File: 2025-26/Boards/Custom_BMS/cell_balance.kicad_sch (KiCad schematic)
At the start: 34 parts

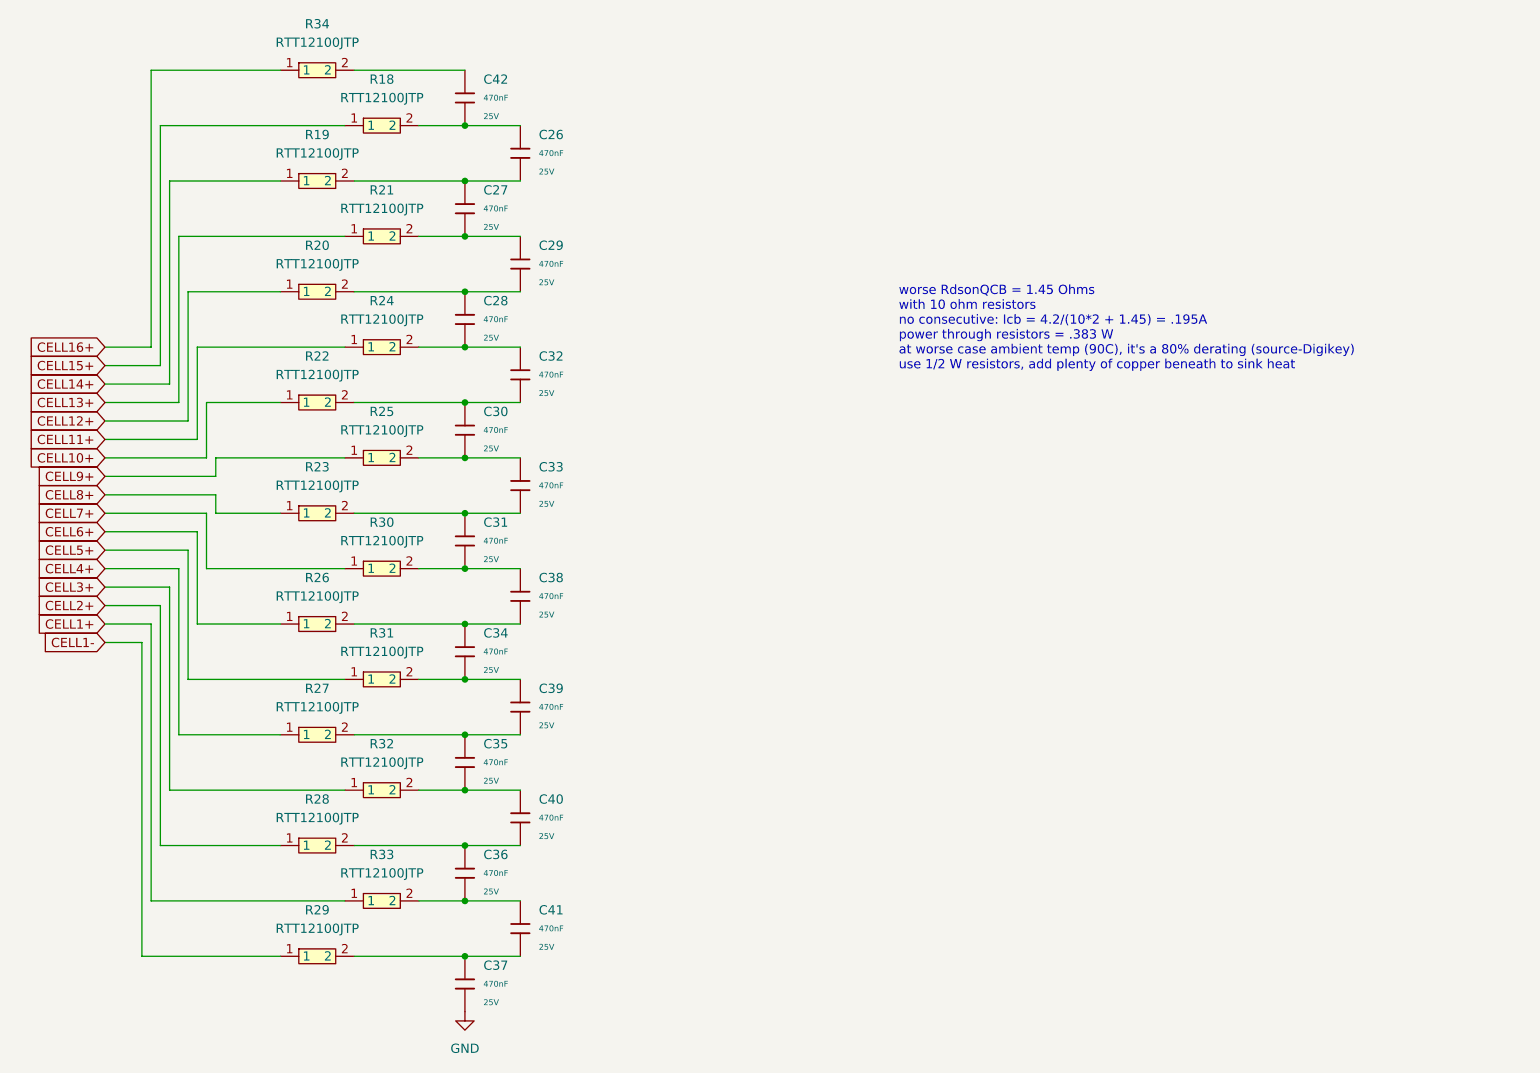
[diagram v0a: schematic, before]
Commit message: fixed some net names
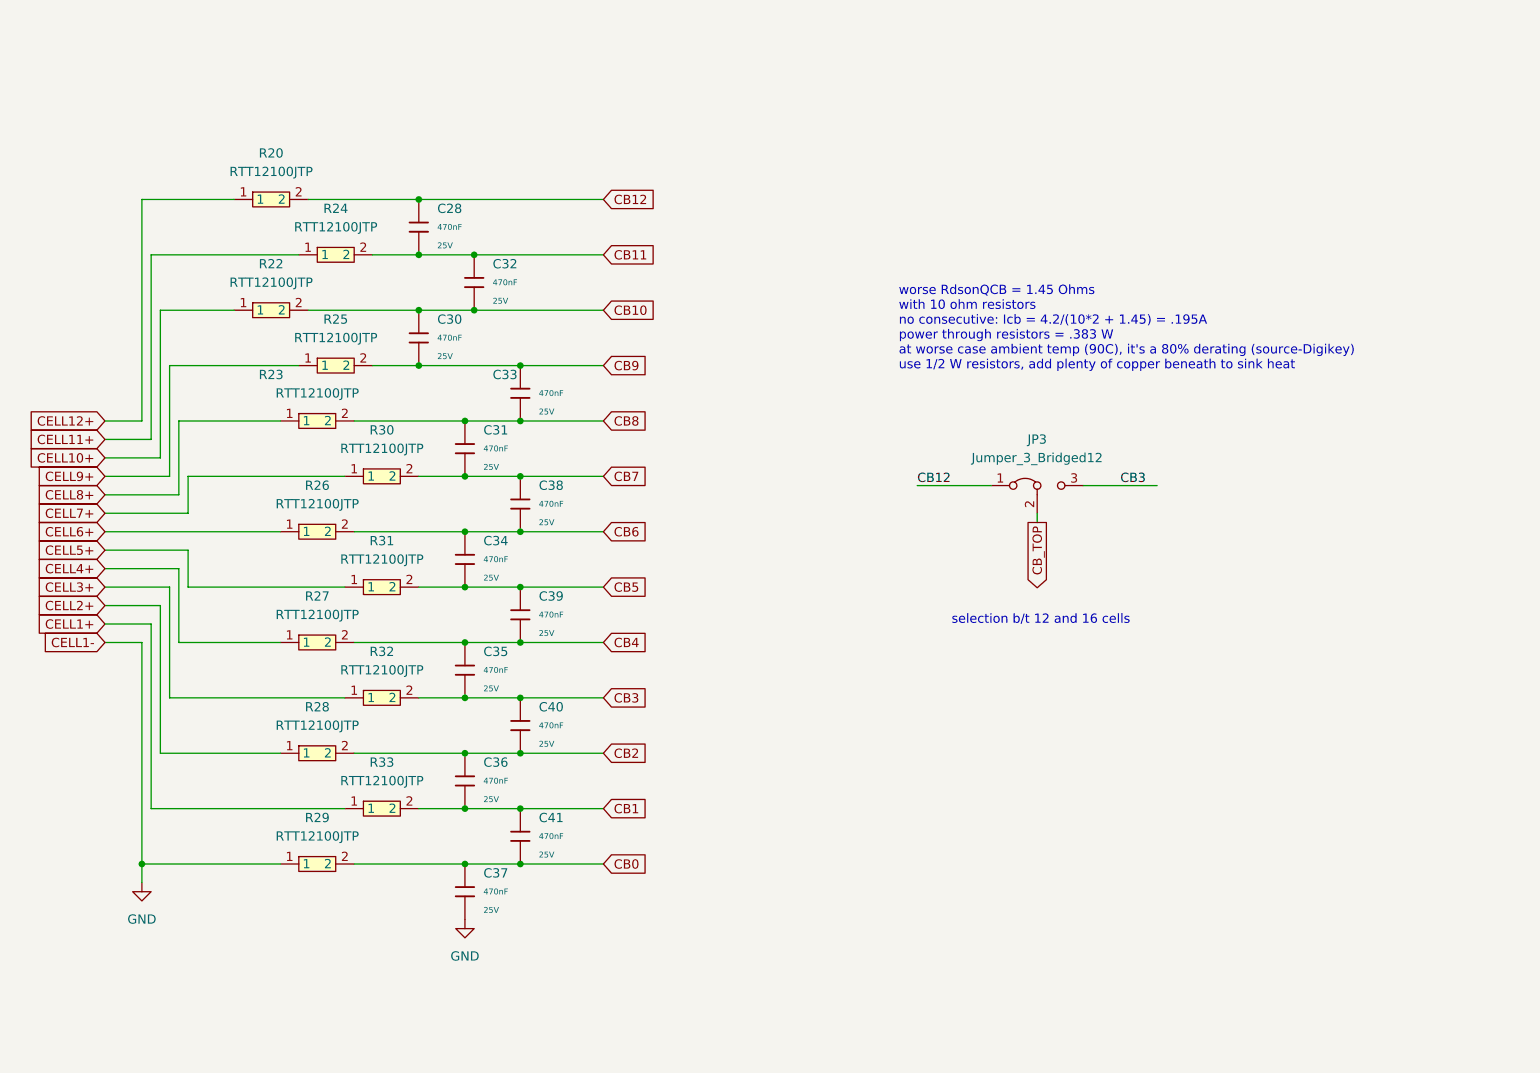
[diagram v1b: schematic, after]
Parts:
- removed C26, C27, C29, C42: 470nF, PCM_JLCPCB:C_0603, symbol PCM_JLCPCB-Capacitors:0603,470nF
- removed R18, R19, R21, R34: RTT12100JTP, easyeda2kicad:R1210, symbol easyeda2kicad:RTT12100JTP
- added JP3: Jumper_3_Bridged12, symbol Jumper:Jumper_3_Bridged12
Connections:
- net CELL1- is gone; now on net GND: R29.1
- net CB6: now reaches C34.1, C38.2, R26.2
- net CB8: now reaches C31.1, C33.2, R23.2
- net CB12: now reaches C28.1, R20.2
- net CB12: now also JP3.1 (A)
- net CB10: now reaches C30.1, C32.2, R22.2
- net CB3: now reaches C35.2, C40.1, R32.2
- net CB3: now also JP3.3 (B)
- net CB2: now reaches C36.1, C40.2, R28.2
- net CB9: now reaches C30.2, C33.1, R25.2
- net CB7: now reaches C31.2, C38.1, R30.2
- net CB11: now reaches C28.2, C32.1, R24.2
- net CB4: now reaches C35.1, C39.2, R27.2
- net CB5: now reaches C34.2, C39.1, R31.2
- net CB0: now reaches C37.1, C41.2, R29.2
- net CB1: now reaches C36.2, C41.1, R33.2
- new net CB_TOP: JP3.2 (C)
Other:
- note added: "selection b/t 12 and 16 cells"
- moved on the sheet: C28, C30, C31, C32, C33, C34, C35, C36, C37, C38, C39, C40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

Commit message: started layout
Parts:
- removed JP3: Jumper_3_Bridged12, symbol Jumper:Jumper_3_Bridged12
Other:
- note removed: "selection b/t 12 and 16 cells"
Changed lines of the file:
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@@
 		)
 	)
-	(text "selection b/t 12 and 16 cells"
-		(exclude_from_sim no)
-		(at 188.468 116.332 0)
-		(effects
-			(font
-				(size 1.27 1.27)
-			)
-		)
-	)
 	(junction
 		(at 109.22 127)
@@
 	(wire
 		(pts
-			(xy 194.31 97.79) (xy 204.47 97.79)
-		)
-		(stroke
-			(width 0)
-			(type default)
-		)
-	)
-	(wire
-		(pts
 			(xy 66.04 91.44) (xy 66.04 66.04)
 		)
@@
 	(wire
 		(pts
-			(xy 187.96 101.6) (xy 187.96 102.87)
-		)
-		(stroke
-			(width 0)
-			(type default)
-		)
-	)
-	(wire
-		(pts
 			(xy 69.85 88.9) (xy 69.85 99.06)
 		)
@@
 	(wire
 		(pts
-			(xy 171.45 97.79) (xy 181.61 97.79)
-		)
-		(stroke
-			(width 0)
-			(type default)
-		)
-	)
-	(wire
-		(pts
 			(xy 116.84 149.86) (xy 128.27 149.86)
 		)
@@
 		)
 	)
-	(label "CB3"
-		(at 199.39 97.79 0)
-		(effects
-			(font
-				(size 1.27 1.27)
-			)
-			(justify left bottom)
-		)
-	)
-	(label "CB12"
-		(at 171.45 97.79 0)
-		(effects
-			(font
-				(size 1.27 1.27)
-			)
-			(justify left bottom)
-		)
-	)
 	(global_label "CELL9+"
 		(shape input)
@@
 		)
 	)
-	(global_label "CB_TOP"
-		(shape output)
-		(at 187.96 102.87 270)
-		(fields_autoplaced yes)
-		(effects
-			(font
-				(size 1.27 1.27)
-			)
-			(justify right)
-		)
-		(property "Intersheetrefs" "${INTERSHEET_REFS}"
-			(at 187.96 112.9309 90)
-			(effects
-				(font
-					(size 1.27 1.27)
-				)
-				(justify right)
-				(hide yes)
-			)
-		)
-	)
 	(global_label "CB11"
 		(shape input)
@@
 					(unit 1)
 				)
-			)
-		)
-	)
-	(symbol
-		(lib_id "Jumper:Jumper_3_Bridged12")
-		(at 187.96 97.79 0)
-		(unit 1)
-		(exclude_from_sim no)
-		(in_bom no)
-		(on_board yes)
-		(dnp no)
-		(fields_autoplaced yes)
-		(property "Reference" "JP3"
-			(at 187.96 91.44 0)
-			(effects
-				(font
-					(size 1.27 1.27)
-				)
-			)
-		)
-		(property "Value" "Jumper_3_Bridged12"
-			(at 187.96 93.98 0)
-			(effects
-				(font
-					(size 1.27 1.27)
-				)
-			)
-		)
-		(property "Footprint" ""
-			(at 187.96 97.79 0)
-			(effects
-				(font
-					(size 1.27 1.27)
-				)
-				(hide yes)
-			)
-		)
-		(property "Datasheet" "~"
-			(at 187.96 97.79 0)
-			(effects
-				(font
-					(size 1.27 1.27)
-				)
-				(hide yes)
-			)
-		)
-		(property "Description" "Jumper, 3-pole, pins 1+2 closed/bridged"
-			(at 187.96 97.79 0)
-			(effects
-				(font
-					(size 1.27 1.27)
-				)
-				(hide yes)
-			)
-		)
-		(pin "2"
-		)
-		(pin "3"
-		)
-		(pin "1"
-		)
-		(instances
-			(project "Custom_BMS"
-				(path "/570d6d9c-ebf5-4f83-96f6-d3309a3e637d/e94a219a-300a-4436-8821-3bf884f472d1"
-					(reference "JP3")
-					(unit 1)
-				)

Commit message: more layout progress
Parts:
- added JP2: Jumper_3_Bridged12, Connector_PinHeader_2.00mm:PinHeader_1x03_P2.00mm_Vertical, symbol Jumper:Jumper_3_Bridged12
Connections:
- new net CB12+: JP2.1 (A)
- new net CB3+: JP2.3 (B)
- new net CB_TOP: JP2.2 (C)
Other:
- note added: "selection b/t 12 and 16 cells"
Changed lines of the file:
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@@
 		)
 	)
+	(text "selection b/t 12 and 16 cells"
+		(exclude_from_sim no)
+		(at 195.072 125.73 0)
+		(effects
+			(font
+				(size 1.27 1.27)
+			)
+		)
+	)
 	(junction
 		(at 109.22 127)
@@
 	(wire
 		(pts
+			(xy 176.53 104.14) (xy 186.69 104.14)
+		)
+		(stroke
+			(width 0)
+			(type default)
+		)
+	)
+	(wire
+		(pts
 			(xy 69.85 109.22) (xy 69.85 119.38)
 		)
@@
 	(wire
 		(pts
+			(xy 193.04 107.95) (xy 193.04 109.22)
+		)
+		(stroke
+			(width 0)
+			(type default)
+		)
+	)
+	(wire
+		(pts
 			(xy 59.69 93.98) (xy 67.31 93.98)
 		)
@@
 	(wire
 		(pts
+			(xy 199.39 104.14) (xy 209.55 104.14)
+		)
+		(stroke
+			(width 0)
+			(type default)
+		)
+	)
+	(wire
+		(pts
 			(xy 116.84 96.52) (xy 128.27 96.52)
 		)
@@
 		)
 	)
+	(label "CB3+"
+		(at 201.93 104.14 0)
+		(effects
+			(font
+				(size 1.27 1.27)
+			)
+			(justify left bottom)
+		)
+	)
+	(label "CB12+"
+		(at 176.53 104.14 0)
+		(effects
+			(font
+				(size 1.27 1.27)
+			)
+			(justify left bottom)
+		)
+	)
+	(global_label "CB_TOP"
+		(shape output)
+		(at 193.04 109.22 270)
+		(fields_autoplaced yes)
+		(effects
+			(font
+				(size 1.27 1.27)
+			)
+			(justify right)
+		)
+		(property "Intersheetrefs" "${INTERSHEET_REFS}"
+			(at 193.04 119.2809 90)
+			(effects
+				(font
+					(size 1.27 1.27)
+				)
+				(justify right)
+				(hide yes)
+			)
+		)
+	)
 	(global_label "CELL9+"
 		(shape input)
@@
 					(unit 1)
 				)
+			)
+		)
+	)
+	(symbol
+		(lib_id "Jumper:Jumper_3_Bridged12")
+		(at 193.04 104.14 0)
+		(unit 1)
+		(exclude_from_sim no)
+		(in_bom no)
+		(on_board yes)
+		(dnp no)
+		(fields_autoplaced yes)
+		(property "Reference" "JP2"
+			(at 193.04 97.79 0)
+			(effects
+				(font
+					(size 1.27 1.27)
+				)
+			)
+		)
+		(property "Value" "Jumper_3_Bridged12"
+			(at 193.04 100.33 0)
+			(effects
+				(font
+					(size 1.27 1.27)
+				)
+			)
+		)
+		(property "Footprint" "Connector_PinHeader_2.00mm:PinHeader_1x03_P2.00mm_Vertical"
+			(at 193.04 104.14 0)
+			(effects
+				(font
+					(size 1.27 1.27)
+				)
+				(hide yes)
+			)
+		)
+		(property "Datasheet" "~"
+			(at 193.04 104.14 0)
+			(effects
+				(font
+					(size 1.27 1.27)
+				)
+				(hide yes)
+			)
+		)
+		(property "Description" "Jumper, 3-pole, pins 1+2 closed/bridged"
+			(at 193.04 104.14 0)
+			(effects
+				(font
+					(size 1.27 1.27)
+				)
+				(hide yes)
+			)
+		)
+		(pin "2"
+		)
+		(pin "3"
+		)
+		(pin "1"
+		)
+		(instances
+			(project "Custom_BMS"
+				(path "/570d6d9c-ebf5-4f83-96f6-d3309a3e637d/e94a219a-300a-4436-8821-3bf884f472d1"
+					(reference "JP2")
+					(unit 1)
+				)

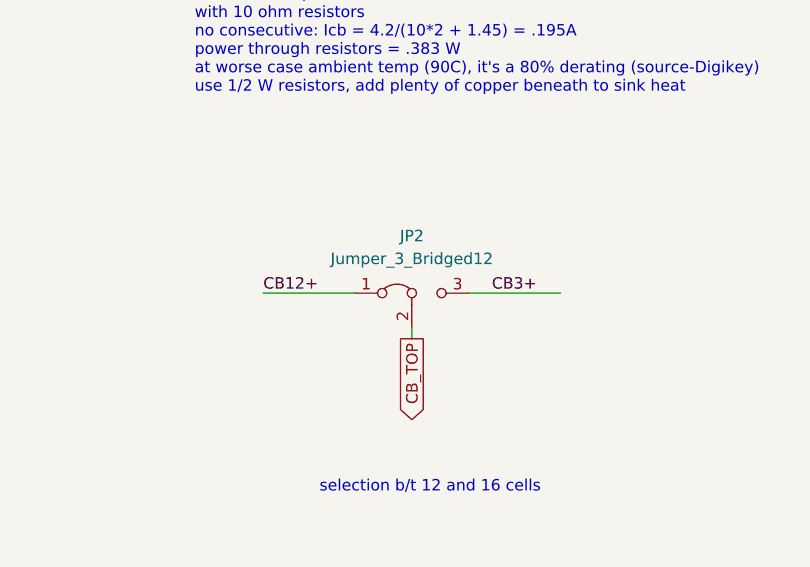
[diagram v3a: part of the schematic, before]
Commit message: finishe difrst draft layout
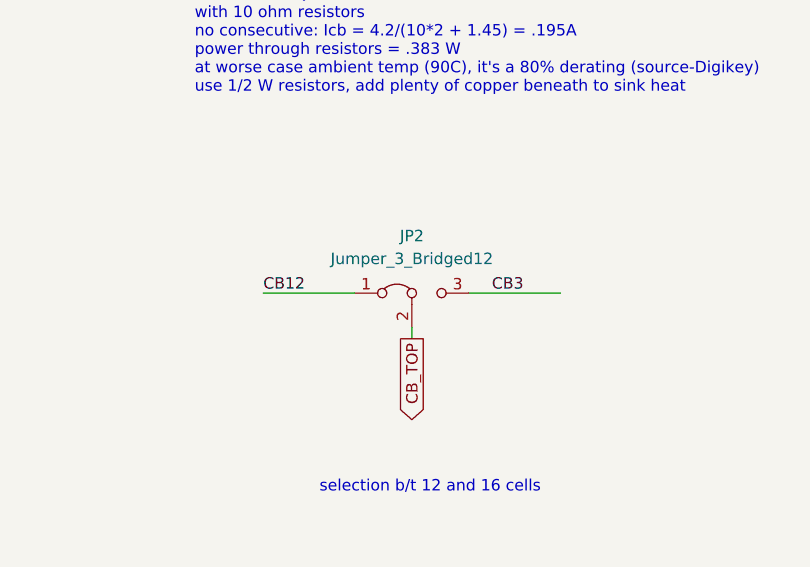
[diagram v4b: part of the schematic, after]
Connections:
- net CB12+ is gone; now on net CB12: JP2.1 (A)
- net CB3+ is gone; now on net CB3: JP2.3 (B)
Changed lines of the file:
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@@
 		)
 	)
-	(label "CB3+"
+	(label "CB3"
 		(at 201.93 104.14 0)
 		(effects
@@
 		)
 	)
-	(label "CB12+"
+	(label "CB12"
 		(at 176.53 104.14 0)
 		(effects
